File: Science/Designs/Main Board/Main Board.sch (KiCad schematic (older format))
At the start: 95 parts, among them J1 I2C_OUT, J10 AIR_SENS, J11 MOISTURE_SENS, J12 LIMIT3, J13 LIMIT2, J14 LIMIT1, J15 SERVO3, J16 SERVO2, J17 SERVO1, J18 MOTOR1_SIG, J19 MOTOR2_SIG, J2 ANE_SENS, J20 MOTOR3_SIG, J4 ENCODER2, J5 ENCODER1, J7 ATMO_SENS, P1 LS7366R, P2 LS7366R, P3 RPI_HEADER, P4 PWR_IN, P5 UV_SENS, P6 DIST_SENS, P7 I2C_TEST, P8 THERMO_SENS, P9 SPI_TEST, U1 SN74HC14N, U2 TLV2544ID, U3 PCA9685, U4 PCA9685, Y1 20MHz, Y2 20MHz

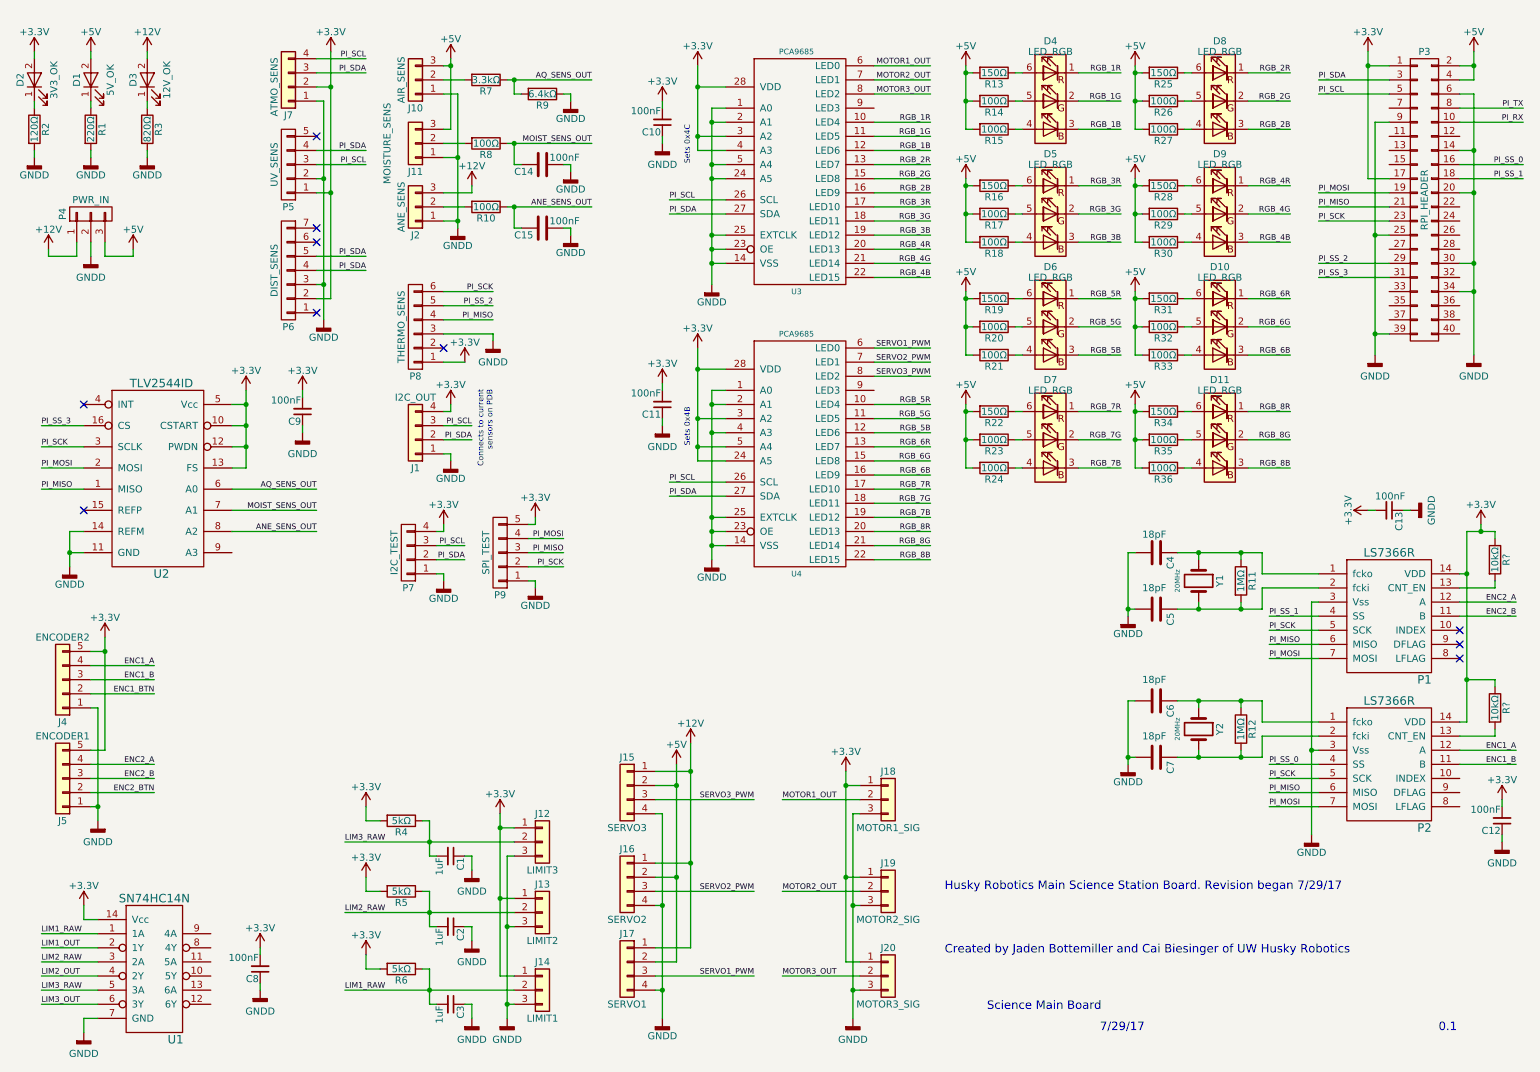
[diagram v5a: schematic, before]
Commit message: Added optocouplers to servo outputs
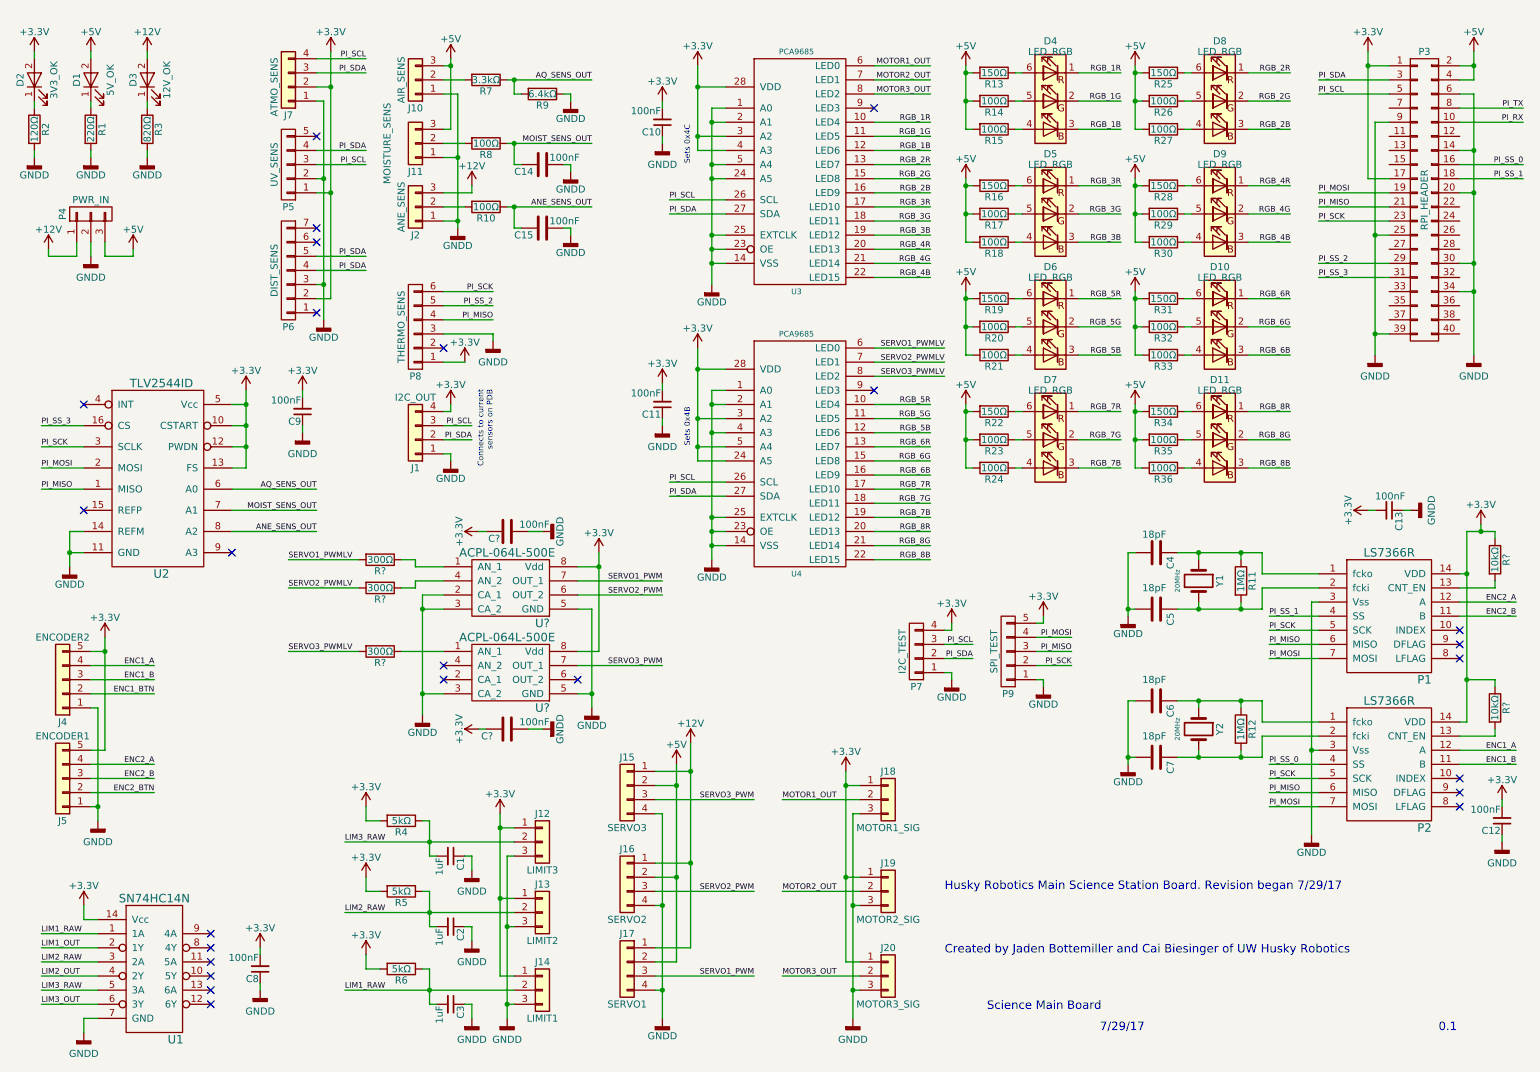
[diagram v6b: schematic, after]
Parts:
- added C? (x2): 100nF, symbol C
- added R? (x3): 300Ω, symbol R
- added U? (x2): ACPL-064L-500E, symbol ACPL-064L-500E
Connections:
- net +3V3: now also C?.1, C?.1, U?.8 (Vdd), U?.8 (Vdd)
- net GNDD: now also C?.2, C?.2, U?.2 (CA_1), U?.3 (CA_2), U?.3 (CA_2), U?.5 (GND), U?.5 (GND)
- net SERVO1_PWM: now also U?.7 (OUT_1); no longer U4.6 (LED0)
- net SERVO2_PWM: now also U?.6 (OUT_2); no longer U4.7 (LED1)
- net SERVO3_PWM: now also U?.7 (OUT_1); no longer U4.8 (LED2)
- new net: R?.1, U?.1 (AN_1) (x2)
- new net: R?.1, U?.4 (AN_2)
- new net SERVO1_PWMLV: R?.2, U4.6 (LED0)
- new net SERVO2_PWMLV: R?.2, U4.7 (LED1)
- new net SERVO3_PWMLV: R?.2, U4.8 (LED2)
- no-connect marks 10 -> 25
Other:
- moved on the sheet: P7, P9
